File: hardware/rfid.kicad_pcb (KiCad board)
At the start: 2 copper layers, 75 x 50 mm, 33 parts, among them P1 CONN_01X02, P2 COMMS, U1 CR95HF

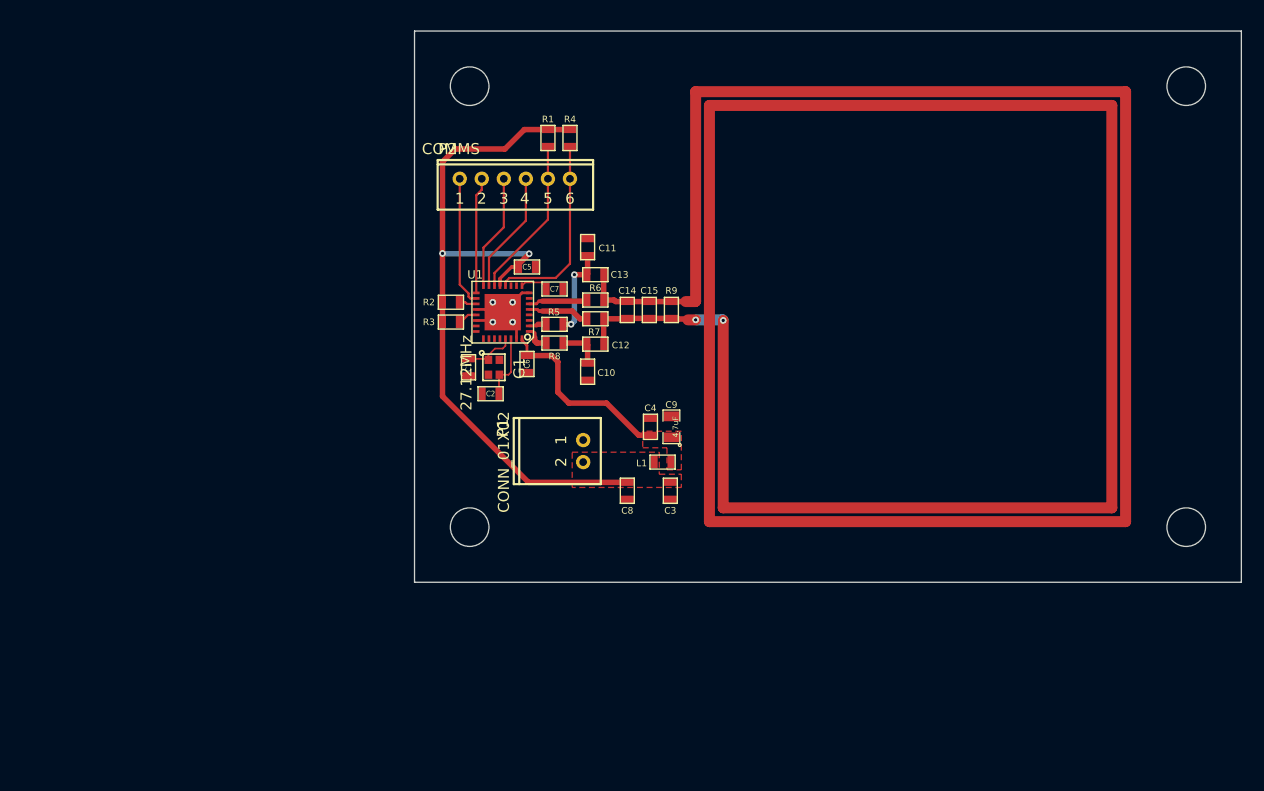
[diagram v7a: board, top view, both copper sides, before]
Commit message: Rounded corners of PCB just because I can. added ground planes and finished routing everything. Added some information text (name, license, github link, etc).
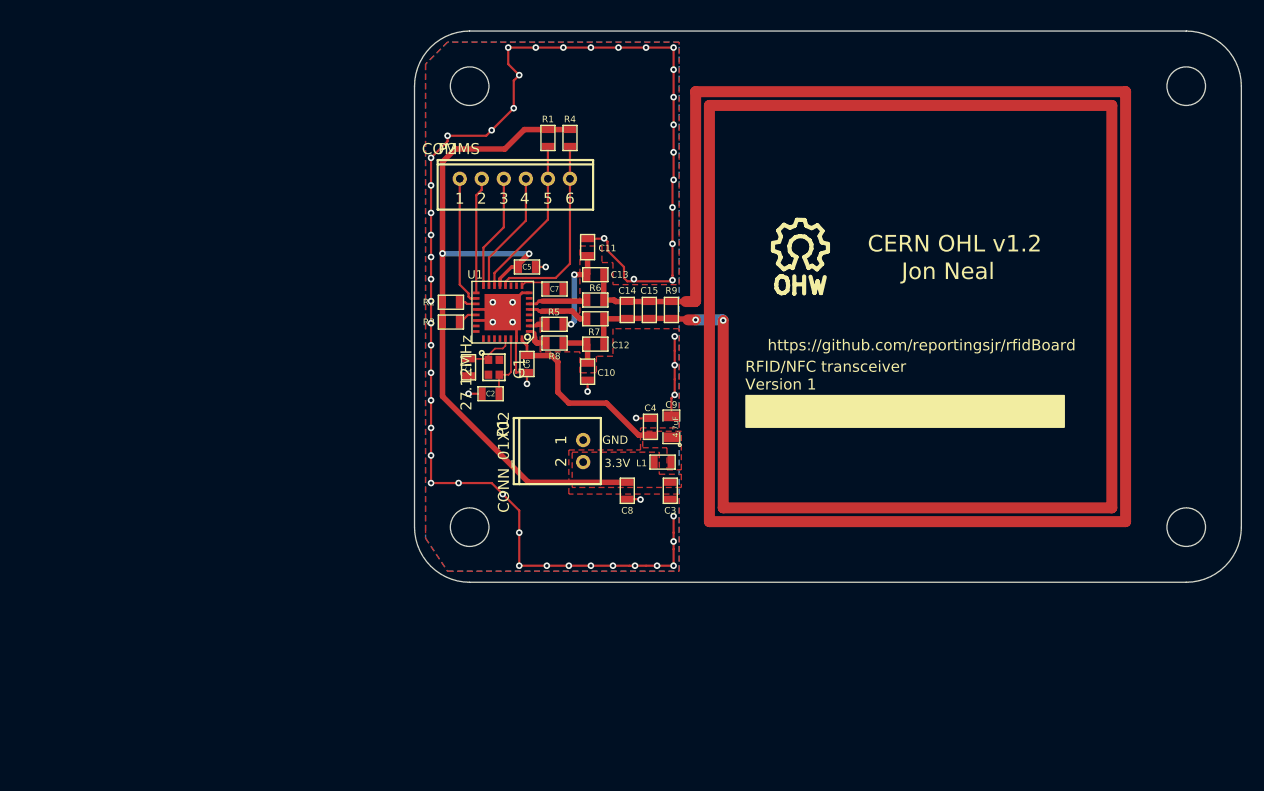
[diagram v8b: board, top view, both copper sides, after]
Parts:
- added SYM: Symbol_OSHW-Logo_SilkScreen_07Jul2012, rfid:Symbol_OHW-Logo_SilkScreen, F.Cu at (191.0, 79.6)
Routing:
- net GND: track 13.5 -> 156.2 mm, vias 4 -> 58
- net (no net): vias 0 -> 3
- added copper zone on B.Cu, net GND
- added copper zone on F.Cu, net GND
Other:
- outline, holes or cut-outs redrawn
- board text added: "3.3V"
- board text added: "CERN OHL v1.2"
- board text added: "GND"
- board text added: "Jon Neal"
- board text added: "RFID/NFC transceiver Version 1"
- board text added: "https://github.com/reportingsjr/rfidBoard"
